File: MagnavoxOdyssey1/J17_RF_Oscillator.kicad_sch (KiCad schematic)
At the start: 22 parts

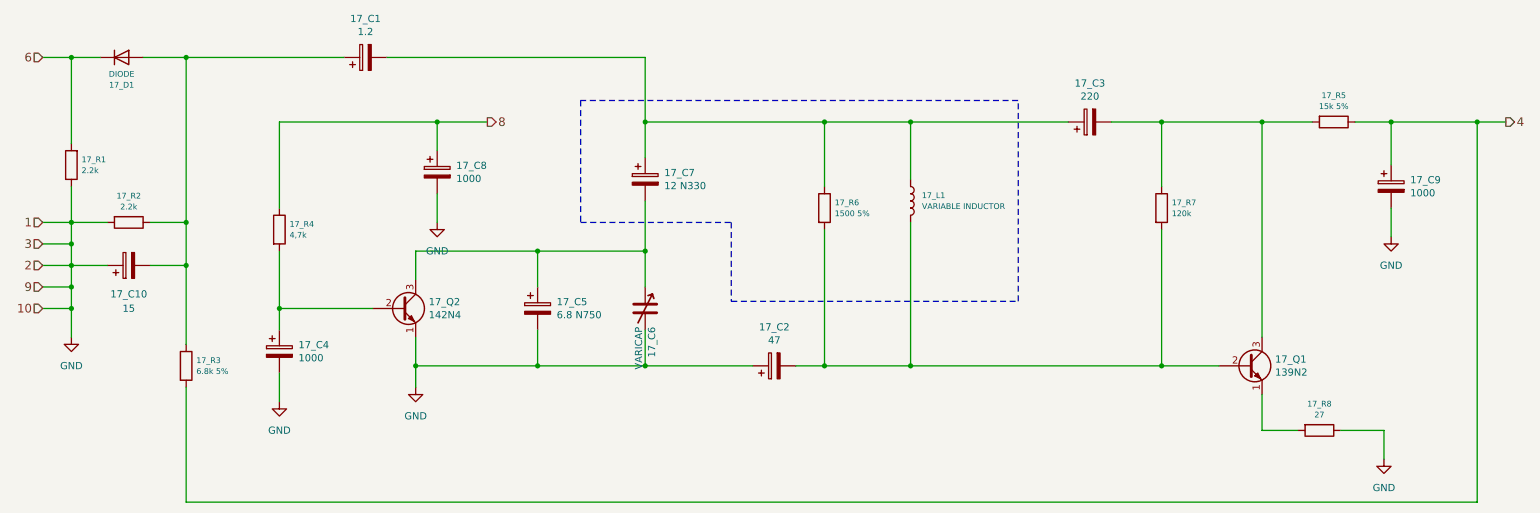
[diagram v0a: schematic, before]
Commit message: update to kicad 9
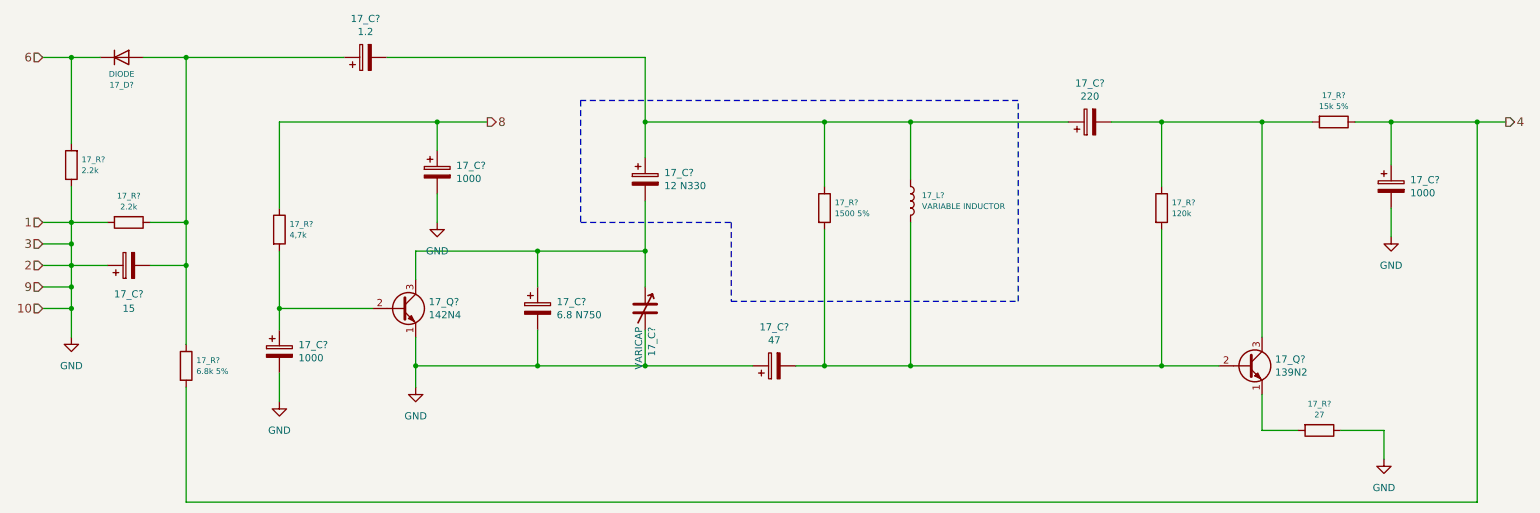
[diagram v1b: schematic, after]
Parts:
- 17_Q?: renamed from 17_Q2; symbol Device:Q_NPN_EBC -> Transistor_BJT:Q_NPN_EBC
- 17_Q?: renamed from 17_Q1; symbol Device:Q_NPN_EBC -> Transistor_BJT:Q_NPN_EBC
- renumbered 17_C2 to 17_C?, 17_C5 to 17_C?, 17_C6 to 17_C?, 17_C4 to 17_C?, 17_C8 to 17_C?, 17_C7 to 17_C?, 17_C1 to 17_C?, 17_C3 to 17_C?, 17_C9 to 17_C?, 17_C10 to 17_C?, 17_D1 to 17_D?, 17_L1 to 17_L?, 17_R4 to 17_R?, 17_R6 to 17_R?, 17_R7 to 17_R?, 17_R8 to 17_R?, 17_R5 to 17_R?, 17_R3 to 17_R?, 17_R2 to 17_R?, 17_R1 to 17_R?
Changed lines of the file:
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@@
 (kicad_sch
-	(version 20231120)
+	(version 20250114)
 	(generator "eeschema")
-	(generator_version "8.0")
+	(generator_version "9.0")
 	(paper "A4")
 	(junction
@@
 	)
 	(symbol
-		(lib_id "Device:Q_NPN_EBC")
+		(lib_id "Transistor_BJT:Q_NPN_EBC")
 		(at 82.55 107.95 0)
 		(unit 1)
@@
 		(on_board yes)
 		(dnp no)
-		(property "Reference" "17_Q2"
+		(property "Reference" "17_Q?"
 			(at 87.4014 106.7816 0)
 			(effects
@@
 		(pin "3"
 		)
+		(instances
+			(project "MagnavoxOdyssey1"
+				(path "/adb6e295-eae5-402e-a614-02a705c3e27c/00000000-0000-0000-0000-0000588c9ee2"
+					(reference "17_Q?")
+					(unit 1)
+				)
+			)
+		)
 	)
 	(symbol
-		(lib_id "Device:Q_NPN_EBC")
+		(lib_id "Transistor_BJT:Q_NPN_EBC")
 		(at 232.41 118.11 0)
 		(unit 1)
@@
 		(on_board yes)
 		(dnp no)
-		(property "Reference" "17_Q1"
+		(property "Reference" "17_Q?"
 			(at 237.2614 116.9416 0)
 			(effects
@@
 		)
 		(pin "3"
+		)
+		(instances
+			(project "MagnavoxOdyssey1"
+				(path "/adb6e295-eae5-402e-a614-02a705c3e27c/00000000-0000-0000-0000-0000588c9ee2"
+					(reference "17_Q?")
+					(unit 1)
+				)
+			)
 		)
 	)
@@
 		(on_board yes)
 		(dnp no)
-		(property "Reference" "17_C2"
+		(property "Reference" "17_C?"
 			(at 148.59 111.252 90)
 			(effects
@@
 		)
 		(pin "2"
+		)
+		(instances
+			(project "MagnavoxOdyssey1"
+				(path "/adb6e295-eae5-402e-a614-02a705c3e27c/00000000-0000-0000-0000-0000588c9ee2"
+					(reference "17_C?")
+					(unit 1)
+				)
+			)
 		)
 	)
@@
 		(on_board yes)
 		(dnp no)
-		(property "Reference" "17_C5"
+		(property "Reference" "17_C?"
 			(at 110.0582 106.7816 0)
 			(effects
@@
 		)
 		(pin "2"
+		)
+		(instances
+			(project "MagnavoxOdyssey1"
+				(path "/adb6e295-eae5-402e-a614-02a705c3e27c/00000000-0000-0000-0000-0000588c9ee2"
+					(reference "17_C?")
+					(unit 1)
+				)
+			)
 		)
 	)
@@
 		(on_board yes)
 		(dnp no)
-		(property "Reference" "17_C6"
+		(property "Reference" "17_C?"
 			(at 126.8984 111.2012 90)
 			(effects
@@
 		)
 		(pin "2"
+		)
+		(instances
+			(project "MagnavoxOdyssey1"
+				(path "/adb6e295-eae5-402e-a614-02a705c3e27c/00000000-0000-0000-0000-0000588c9ee2"
+					(reference "17_C?")
+					(unit 1)
+				)
+			)
 		)
 	)
@@
 		(on_board yes)
 		(dnp no)
-		(property "Reference" "17_C4"
+		(property "Reference" "17_C?"
 			(at 64.3382 114.4016 0)
 			(effects
@@
 		)
 		(pin "2"
+		)
+		(instances
+			(project "MagnavoxOdyssey1"
+				(path "/adb6e295-eae5-402e-a614-02a705c3e27c/00000000-0000-0000-0000-0000588c9ee2"
+					(reference "17_C?")
+					(unit 1)
+				)
+			)
 		)
 	)
@@
 		(on_board yes)
 		(dnp no)
-		(property "Reference" "17_R4"
+		(property "Reference" "17_R?"
 			(at 62.7634 93.0148 0)
 			(effects
@@
 		)
 		(pin "2"
+		)
+		(instances
+			(project "MagnavoxOdyssey1"
+				(path "/adb6e295-eae5-402e-a614-02a705c3e27c/00000000-0000-0000-0000-0000588c9ee2"
+					(reference "17_R?")
+					(unit 1)
+				)
+			)
 		)
 	)
@@
 		(on_board yes)
 		(dnp no)
-		(property "Reference" "17_C8"
+		(property "Reference" "17_C?"
 			(at 92.2782 82.6516 0)
 			(effects
@@
 		)
 		(pin "2"
+		)
+		(instances
+			(project "MagnavoxOdyssey1"
+				(path "/adb6e295-eae5-402e-a614-02a705c3e27c/00000000-0000-0000-0000-0000588c9ee2"
+					(reference "17_C?")
+					(unit 1)
+				)
+			)
 		)
 	)
@@
 		(on_board yes)
 		(dnp no)
-		(property "Reference" "17_C7"
+		(property "Reference" "17_C?"
 			(at 129.1082 83.9216 0)
 			(effects
@@
 		)
 		(pin "2"
+		)
+		(instances
+			(project "MagnavoxOdyssey1"
+				(path "/adb6e295-eae5-402e-a614-02a705c3e27c/00000000-0000-0000-0000-0000588c9ee2"
+					(reference "17_C?")
+					(unit 1)
+				)
+			)
 		)
 	)
@@
 		(on_board yes)
 		(dnp no)
-		(property "Reference" "17_C1"
+		(property "Reference" "17_C?"
 			(at 76.2 56.642 90)
 			(effects
@@
 		)
 		(pin "2"
+		)
+		(instances
+			(project "MagnavoxOdyssey1"
+				(path "/adb6e295-eae5-402e-a614-02a705c3e27c/00000000-0000-0000-0000-0000588c9ee2"
+					(reference "17_C?")
+					(unit 1)
+				)
+			)
 		)
 	)
@@
 		(on_board yes)
 		(dnp no)
-		(property "Reference" "17_R6"
+		(property "Reference" "17_R?"
 			(at 159.2834 89.2048 0)
 			(effects
@@
 		)
 		(pin "2"
+		)
+		(instances
+			(project "MagnavoxOdyssey1"
+				(path "/adb6e295-eae5-402e-a614-02a705c3e27c/00000000-0000-0000-0000-0000588c9ee2"
+					(reference "17_R?")
+					(unit 1)
+				)
+			)
 		)
 	)
@@
 		(on_board yes)
 		(dnp no)
-		(property "Reference" "17_L1"
+		(property "Reference" "17_L?"
 			(at 174.7266 87.9348 0)
 			(effects
@@
 		)
 		(pin "2"
+		)
+		(instances
+			(project "MagnavoxOdyssey1"
+				(path "/adb6e295-eae5-402e-a614-02a705c3e27c/00000000-0000-0000-0000-0000588c9ee2"
+					(reference "17_L?")
+					(unit 1)
+				)
+			)
 		)
 	)
@@
 		(on_board yes)
 		(dnp no)
-		(property "Reference" "17_C3"
+		(property "Reference" "17_C?"
 			(at 204.47 68.072 90)
 			(effects
@@
 		)
 		(pin "2"
+		)
+		(instances
+			(project "MagnavoxOdyssey1"
+				(path "/adb6e295-eae5-402e-a614-02a705c3e27c/00000000-0000-0000-0000-0000588c9ee2"
+					(reference "17_C?")
+					(unit 1)
+				)
+			)
 		)
 	)
@@
 		(on_board yes)
 		(dnp no)
-		(property "Reference" "17_R7"
+		(property "Reference" "17_R?"
 			(at 218.9734 89.2048 0)
 			(effects
@@
 		)
 		(pin "2"
+		)
+		(instances
+			(project "MagnavoxOdyssey1"
+				(path "/adb6e295-eae5-402e-a614-02a705c3e27c/00000000-0000-0000-0000-0000588c9ee2"
+					(reference "17_R?")
+					(unit 1)
+				)
+			)
 		)
 	)
@@
 		(on_board yes)
 		(dnp no)
-		(property "Reference" "17_R8"
+		(property "Reference" "17_R?"
 			(at 245.11 124.841 90)
 			(effects
@@
 		)
 		(pin "2"
+		)
+		(instances
+			(project "MagnavoxOdyssey1"
+				(path "/adb6e295-eae5-402e-a614-02a705c3e27c/00000000-0000-0000-0000-0000588c9ee2"
+					(reference "17_R?")
+					(unit 1)
+				)
+			)
 		)
 	)
@@
 		(on_board yes)
 		(dnp no)
-		(property "Reference" "17_R5"
+		(property "Reference" "17_R?"
 			(at 247.65 70.231 90)
 			(effects
@@
 		)
 		(pin "2"
+		)
+		(instances
+			(project "MagnavoxOdyssey1"
+				(path "/adb6e295-eae5-402e-a614-02a705c3e27c/00000000-0000-0000-0000-0000588c9ee2"
+					(reference "17_R?")
+					(unit 1)
+				)
+			)
 		)
 	)
@@
 		(on_board yes)
 		(dnp no)
-		(property "Reference" "17_C9"
+		(property "Reference" "17_C?"
 			(at 261.1882 85.1916 0)
 			(effects
@@
 		)
 		(pin "2"
+		)
+		(instances
+			(project "MagnavoxOdyssey1"
+				(path "/adb6e295-eae5-402e-a614-02a705c3e27c/00000000-0000-0000-0000-0000588c9ee2"
+					(reference "17_C?")
+					(unit 1)
+				)
+			)
 		)
 	)
@@
 		(on_board yes)
 		(dnp no)
-		(property "Reference" "17_R3"
+		(property "Reference" "17_R?"
 			(at 46.2534 117.1448 0)
 			(effects
@@
 		)
 		(pin "2"
+		)
+		(instances
+			(project "MagnavoxOdyssey1"
+				(path "/adb6e295-eae5-402e-a614-02a705c3e27c/00000000-0000-0000-0000-0000588c9ee2"
+					(reference "17_R?")
+					(unit 1)
+				)
+			)
 		)
 	)
@@
 		(on_board yes)
 		(dnp no)
-		(property "Reference" "17_C10"
+		(property "Reference" "17_C?"
 			(at 34.29 105.41 90)
 			(effects
@@
 		)
 		(pin "2"
+		)
+		(instances
+			(project "MagnavoxOdyssey1"
+				(path "/adb6e295-eae5-402e-a614-02a705c3e27c/00000000-0000-0000-0000-0000588c9ee2"
+					(reference "17_C?")
+					(unit 1)
+				)
+			)
 		)
 	)
@@
 		(on_board yes)
 		(dnp no)
-		(property "Reference" "17_R2"
+		(property "Reference" "17_R?"
 			(at 34.29 88.011 90)
 			(effects
@@
 		)
 		(pin "2"
+		)
+		(instances
+			(project "MagnavoxOdyssey1"
+				(path "/adb6e295-eae5-402e-a614-02a705c3e27c/00000000-0000-0000-0000-0000588c9ee2"
+					(reference "17_R?")
+					(unit 1)
+				)
+			)
 		)
 	)
@@
 		(on_board yes)
 		(dnp no)
-		(property "Reference" "17_R1"
+		(property "Reference" "17_R?"
 			(at 25.9334 81.5848 0)
 			(effects
@@
 		)
 		(pin "2"
+		)
+		(instances
+			(project "MagnavoxOdyssey1"
+				(path "/adb6e295-eae5-402e-a614-02a705c3e27c/00000000-0000-0000-0000-0000588c9ee2"
+					(reference "17_R?")
+					(unit 1)
+				)
+			)
 		)
 	)
@@
 		(on_board yes)
 		(dnp no)
-		(property "Reference" "17_D1"
+		(property "Reference" "17_D?"
 			(at 33.02 68.3768 0)
 			(effects
@@
 		(pin "2"
 		)
-	)
+		(instances
+			(project "MagnavoxOdyssey1"
+				(path "/adb6e295-eae5-402e-a614-02a705c3e27c/00000000-0000-0000-0000-0000588c9ee2"
+					(reference "17_D?")
+					(unit 1)
+				)
+			)
+		)
+	)

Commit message: annotate
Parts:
- gave numbers to parts that had none: 22
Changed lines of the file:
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@@
 		(on_board yes)
 		(dnp no)
-		(property "Reference" "17_Q?"
+		(property "Reference" "17_Q1"
 			(at 87.4014 106.7816 0)
 			(effects
@@
 			(project "MagnavoxOdyssey1"
 				(path "/adb6e295-eae5-402e-a614-02a705c3e27c/00000000-0000-0000-0000-0000588c9ee2"
-					(reference "17_Q?")
+					(reference "17_Q1")
 					(unit 1)
 				)
@@
 		(on_board yes)
 		(dnp no)
-		(property "Reference" "17_Q?"
+		(property "Reference" "17_Q2"
 			(at 237.2614 116.9416 0)
 			(effects
@@
 			(project "MagnavoxOdyssey1"
 				(path "/adb6e295-eae5-402e-a614-02a705c3e27c/00000000-0000-0000-0000-0000588c9ee2"
-					(reference "17_Q?")
+					(reference "17_Q2")
 					(unit 1)
 				)
@@
 		(on_board yes)
 		(dnp no)
-		(property "Reference" "17_C?"
+		(property "Reference" "17_C10"
 			(at 148.59 111.252 90)
 			(effects
@@
 			(project "MagnavoxOdyssey1"
 				(path "/adb6e295-eae5-402e-a614-02a705c3e27c/00000000-0000-0000-0000-0000588c9ee2"
-					(reference "17_C?")
+					(reference "17_C10")
 					(unit 1)
 				)
@@
 		(on_board yes)
 		(dnp no)
-		(property "Reference" "17_C?"
+		(property "Reference" "17_C7"
 			(at 110.0582 106.7816 0)
 			(effects
@@
 			(project "MagnavoxOdyssey1"
 				(path "/adb6e295-eae5-402e-a614-02a705c3e27c/00000000-0000-0000-0000-0000588c9ee2"
-					(reference "17_C?")
+					(reference "17_C7")
 					(unit 1)
 				)
@@
 		(on_board yes)
 		(dnp no)
-		(property "Reference" "17_C?"
+		(property "Reference" "17_C8"
 			(at 126.8984 111.2012 90)
 			(effects
@@
 			(project "MagnavoxOdyssey1"
 				(path "/adb6e295-eae5-402e-a614-02a705c3e27c/00000000-0000-0000-0000-0000588c9ee2"
-					(reference "17_C?")
+					(reference "17_C8")
 					(unit 1)
 				)
@@
 		(on_board yes)
 		(dnp no)
-		(property "Reference" "17_C?"
+		(property "Reference" "17_C9"
 			(at 64.3382 114.4016 0)
 			(effects
@@
 			(project "MagnavoxOdyssey1"
 				(path "/adb6e295-eae5-402e-a614-02a705c3e27c/00000000-0000-0000-0000-0000588c9ee2"
-					(reference "17_C?")
+					(reference "17_C9")
 					(unit 1)
 				)
@@
 		(on_board yes)
 		(dnp no)
-		(property "Reference" "17_R?"
+		(property "Reference" "17_R6"
 			(at 62.7634 93.0148 0)
 			(effects
@@
 			(project "MagnavoxOdyssey1"
 				(path "/adb6e295-eae5-402e-a614-02a705c3e27c/00000000-0000-0000-0000-0000588c9ee2"
-					(reference "17_R?")
+					(reference "17_R6")
 					(unit 1)
 				)
@@
 		(on_board yes)
 		(dnp no)
-		(property "Reference" "17_C?"
+		(property "Reference" "17_C3"
 			(at 92.2782 82.6516 0)
 			(effects
@@
 			(project "MagnavoxOdyssey1"
 				(path "/adb6e295-eae5-402e-a614-02a705c3e27c/00000000-0000-0000-0000-0000588c9ee2"
-					(reference "17_C?")
+					(reference "17_C3")
 					(unit 1)
 				)
@@
 		(on_board yes)
 		(dnp no)
-		(property "Reference" "17_C?"
+		(property "Reference" "17_C4"
 			(at 129.1082 83.9216 0)
 			(effects
@@
 			(project "MagnavoxOdyssey1"
 				(path "/adb6e295-eae5-402e-a614-02a705c3e27c/00000000-0000-0000-0000-0000588c9ee2"
-					(reference "17_C?")
+					(reference "17_C4")
 					(unit 1)
 				)
@@
 		(on_board yes)
 		(dnp no)
-		(property "Reference" "17_C?"
+		(property "Reference" "17_C1"
 			(at 76.2 56.642 90)
 			(effects
@@
 			(project "MagnavoxOdyssey1"
 				(path "/adb6e295-eae5-402e-a614-02a705c3e27c/00000000-0000-0000-0000-0000588c9ee2"
-					(reference "17_C?")
+					(reference "17_C1")
 					(unit 1)
 				)
@@
 		(on_board yes)
 		(dnp no)
-		(property "Reference" "17_R?"
+		(property "Reference" "17_R3"
 			(at 159.2834 89.2048 0)
 			(effects
@@
 			(project "MagnavoxOdyssey1"
 				(path "/adb6e295-eae5-402e-a614-02a705c3e27c/00000000-0000-0000-0000-0000588c9ee2"
-					(reference "17_R?")
+					(reference "17_R3")
 					(unit 1)
 				)
@@
 		(on_board yes)
 		(dnp no)
-		(property "Reference" "17_L?"
+		(property "Reference" "17_L1"
 			(at 174.7266 87.9348 0)
 			(effects
@@
 			(project "MagnavoxOdyssey1"
 				(path "/adb6e295-eae5-402e-a614-02a705c3e27c/00000000-0000-0000-0000-0000588c9ee2"
-					(reference "17_L?")
+					(reference "17_L1")
 					(unit 1)
 				)
@@
 		(on_board yes)
 		(dnp no)
-		(property "Reference" "17_C?"
+		(property "Reference" "17_C2"
 			(at 204.47 68.072 90)
 			(effects
@@
 			(project "MagnavoxOdyssey1"
 				(path "/adb6e295-eae5-402e-a614-02a705c3e27c/00000000-0000-0000-0000-0000588c9ee2"
-					(reference "17_C?")
+					(reference "17_C2")
 					(unit 1)
 				)
@@
 		(on_board yes)
 		(dnp no)
-		(property "Reference" "17_R?"
+		(property "Reference" "17_R4"
 			(at 218.9734 89.2048 0)
 			(effects
@@
 			(project "MagnavoxOdyssey1"
 				(path "/adb6e295-eae5-402e-a614-02a705c3e27c/00000000-0000-0000-0000-0000588c9ee2"
-					(reference "17_R?")
+					(reference "17_R4")
 					(unit 1)
 				)
@@
 		(on_board yes)
 		(dnp no)
-		(property "Reference" "17_R?"
+		(property "Reference" "17_R8"
 			(at 245.11 124.841 90)
 			(effects
@@
 			(project "MagnavoxOdyssey1"
 				(path "/adb6e295-eae5-402e-a614-02a705c3e27c/00000000-0000-0000-0000-0000588c9ee2"
-					(reference "17_R?")
+					(reference "17_R8")
 					(unit 1)
 				)
@@
 		(on_board yes)
 		(dnp no)
-		(property "Reference" "17_R?"
+		(property "Reference" "17_R1"
 			(at 247.65 70.231 90)
 			(effects
@@
 			(project "MagnavoxOdyssey1"
 				(path "/adb6e295-eae5-402e-a614-02a705c3e27c/00000000-0000-0000-0000-0000588c9ee2"
-					(reference "17_R?")
+					(reference "17_R1")
 					(unit 1)
 				)
@@
 		(on_board yes)
 		(dnp no)
-		(property "Reference" "17_C?"
+		(property "Reference" "17_C5"
 			(at 261.1882 85.1916 0)
 			(effects
@@
 			(project "MagnavoxOdyssey1"
 				(path "/adb6e295-eae5-402e-a614-02a705c3e27c/00000000-0000-0000-0000-0000588c9ee2"
-					(reference "17_C?")
+					(reference "17_C5")
 					(unit 1)
 				)
@@
 		(on_board yes)
 		(dnp no)
-		(property "Reference" "17_R?"
+		(property "Reference" "17_R7"
 			(at 46.2534 117.1448 0)
 			(effects
@@
 			(project "MagnavoxOdyssey1"
 				(path "/adb6e295-eae5-402e-a614-02a705c3e27c/00000000-0000-0000-0000-0000588c9ee2"
-					(reference "17_R?")
+					(reference "17_R7")
 					(unit 1)
 				)
@@
 		(on_board yes)
 		(dnp no)
-		(property "Reference" "17_C?"
+		(property "Reference" "17_C6"
 			(at 34.29 105.41 90)
 			(effects
@@
 			(project "MagnavoxOdyssey1"
 				(path "/adb6e295-eae5-402e-a614-02a705c3e27c/00000000-0000-0000-0000-0000588c9ee2"
-					(reference "17_C?")
+					(reference "17_C6")
 					(unit 1)
 				)
@@
 		(on_board yes)
 		(dnp no)
-		(property "Reference" "17_R?"
+		(property "Reference" "17_R5"
 			(at 34.29 88.011 90)
 			(effects
@@
 			(project "MagnavoxOdyssey1"
 				(path "/adb6e295-eae5-402e-a614-02a705c3e27c/00000000-0000-0000-0000-0000588c9ee2"
-					(reference "17_R?")
+					(reference "17_R5")
 					(unit 1)
 				)
@@
 		(on_board yes)
 		(dnp no)
-		(property "Reference" "17_R?"
+		(property "Reference" "17_R2"
 			(at 25.9334 81.5848 0)
 			(effects
@@
 			(project "MagnavoxOdyssey1"
 				(path "/adb6e295-eae5-402e-a614-02a705c3e27c/00000000-0000-0000-0000-0000588c9ee2"
-					(reference "17_R?")
+					(reference "17_R2")
 					(unit 1)
 				)
@@
 		(on_board yes)
 		(dnp no)
-		(property "Reference" "17_D?"
+		(property "Reference" "17_D1"
 			(at 33.02 68.3768 0)
 			(effects
@@
 			(project "MagnavoxOdyssey1"
 				(path "/adb6e295-eae5-402e-a614-02a705c3e27c/00000000-0000-0000-0000-0000588c9ee2"
-					(reference "17_D?")
-					(unit 1)
-				)
+					(reference "17_D1")
+					(unit 1)
+				)

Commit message: accurate resistors
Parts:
- 17_R1: value 15k 5% -> 15k
- 17_R3: value 1500 5% -> 1500
- 17_R7: value 6.8k 5% -> 6.8k
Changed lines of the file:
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@@
 			)
 		)
-		(property "Value" "1500 5%"
+		(property "Value" "1500"
 			(at 159.2834 91.1352 0)
 			(effects
@@
 			)
 		)
-		(property "Value" "15k 5%"
+		(property "Value" "15k"
 			(at 247.65 72.1614 90)
 			(effects
@@
 			)
 		)
-		(property "Value" "6.8k 5%"
+		(property "Value" "6.8k"
 			(at 46.2534 119.0752 0)
 			(effects
